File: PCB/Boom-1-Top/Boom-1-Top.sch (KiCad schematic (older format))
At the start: 983 parts, among them J1 DEBUG, J10 PIC_DEBUG, J11 PIC_DEBUG, J12 PIC_DEBUG, J13 PIC_DEBUG, J14 PIC_DEBUG, J15 USB_B_Micro, J16 SD_Card, J17 BT_DEBUG, J18 12V Supply, J19 3V3 Bypass, J2 MIDI IN, J20 5V Bypass, J21 Env +12V Supply, J22 Env -12V Supply, J23 OLEDConn, J3 MIDI OUT, J37 Osc1Conn, J38 Osc2Conn, J39 SubNoiseConn, J4 PIC_DEBUG, J40 FiltConn2, J41 EnvGenConn2, J42 EnvGenConn1, J43 FXConn1, J44 FiltConn1, J45 FXConn2, J46 EnvGenConn3, J5 PIC_DEBUG, J6 PIC_DEBUG, J7 PIC_DEBUG, J8 PIC_DEBUG, J9 PIC_DEBUG, Q1 AO3401A, Q2 AO3401A, SW1 Osc1SawEncoder, SW10 SubToOsc2FiltEncoder, SW11 Osc1ToOsc2FiltEncoder, SW12 Osc1FiltFreqEncoder, SW13 Osc2FiltFreqEncoder, SW14 SubFiltFreqEncoder, SW15 OscFiltEnvAttackEncoder, SW16 SubFiltEnvAttackEncoder, SW17 Osc1FiltResEncoder, SW18 Osc2FiltResEncoder, SW19 SubFiltResEncoder, SW2 Osc1SqrEncoder, SW20 OscFiltEnvDecayEncoder, SW21 SubFiltEnvDecayEncoder, SW22 OscFiltEnvSustainEncoder, SW23 SubFiltEnvSustainEncoder, SW24 Osc1DriveEncoder, SW25 Osc2DistortionEncoder, SW26 OscFiltEnvReleaseEncoder, SW27 SubFiltEnvReleaseEncoder, SW28 FXWetDryEncoder, SW29 SubAmpEnvAttackEncoder, SW3 Rotary_Encoder, SW30 OscAmpEnvAttackEncoder, SW31 FXControl1Encoder, SW32 SubAmpEnvDecayEncoder, SW33 OscAmpEnvDecayEncoder, SW34 FXControl2Encoder, SW35 SubAmpEnvSustainEncoder, SW36 OscAmpEnvSustainEncoder, SW37 FXControl3Encoder, SW38 FXFeedbackEncoder, SW39 SubAmpEnvReleaseEncoder, SW4 Rotary_Encoder_Switch, SW40 OscAmpEnvReleaseEncoder, SW41 Reset, SW42 SW_Push, SW43 Reset, SW44 SW_Push, SW45 SW_Push, SW46 SW_Push, SW47 SW_Push, SW48 SW_Push, SW49 SW_Push, SW5 Rotary_Encoder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

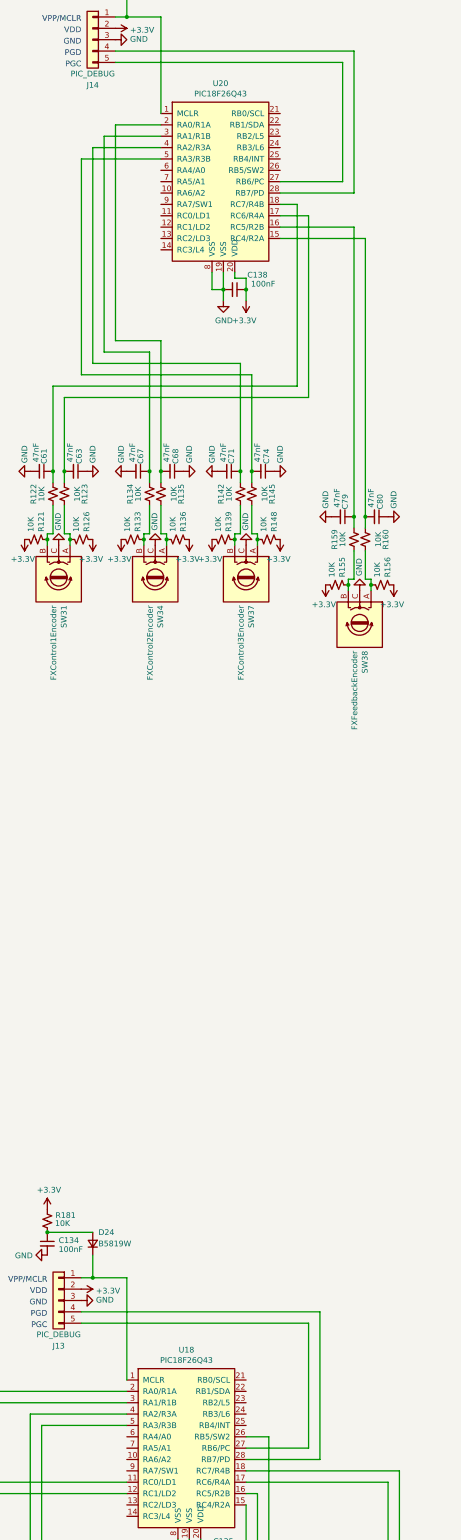
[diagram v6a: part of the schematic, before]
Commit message: U18 PIC i2c
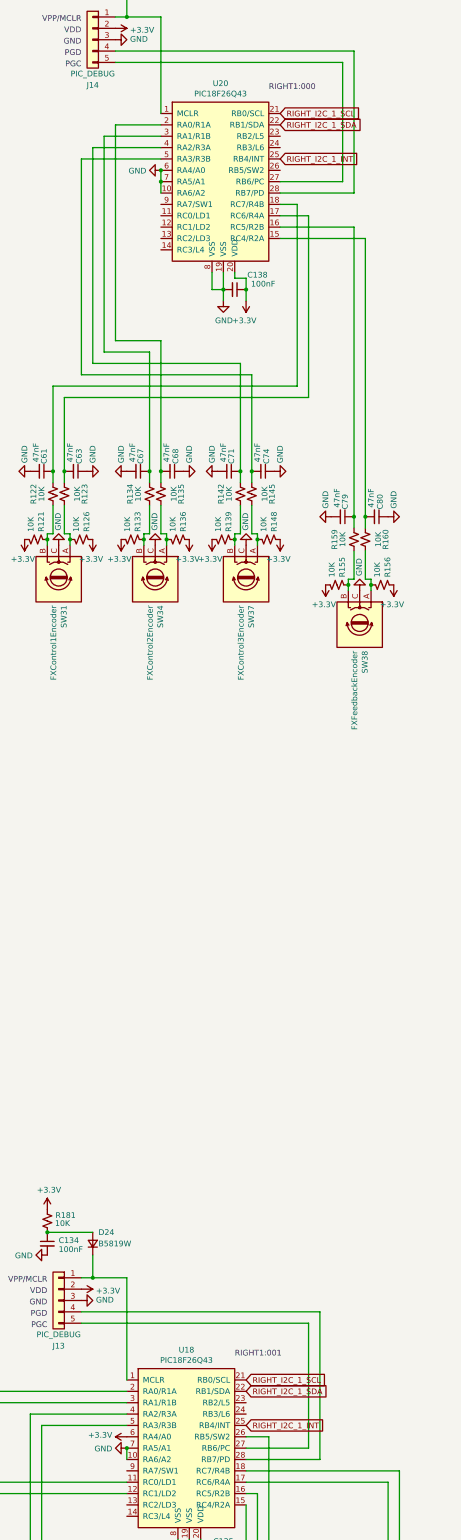
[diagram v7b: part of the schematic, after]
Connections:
- net +3V3: now also U18.6 (RA4/A0)
- net GND: now also U18.10 (RA6/A2), U18.7 (RA5/A1), U20.10 (RA6/A2), U20.6 (RA4/A0), U20.7 (RA5/A1)
- net RIGHT_I2C_1_INT: now also U18.25 (RB4/INT), U20.25 (RB4/INT)
- net RIGHT_I2C_1_SCL: now also U18.21 (RB0/SCL), U20.21 (RB0/SCL)
- net RIGHT_I2C_1_SDA: now also U18.22 (RB1/SDA), U20.22 (RB1/SDA)
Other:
- note added: "RIGHT1:000"
- note added: "RIGHT1:001"
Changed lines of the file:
@@
 LEFT_I2C_3_SCL
 $Comp
-L power:GND #PWR?
+L power:GND #PWR0909
 U 1 1 62205F51
 P 37650 14650
-F 0 "#PWR?" H 37650 14400 50  0001 C CNN
+F 0 "#PWR0909" H 37650 14400 50  0001 C CNN
 F 1 "GND" V 37655 14522 50  0000 R CNN
 F 2 "" H 37650 14650 50  0001 C CNN
@@
 RIGHT0:000
 $Comp
-L power:GND #PWR?
+L power:GND #PWR0910
 U 1 1 60DF9D17
 P 44250 3050
-F 0 "#PWR?" H 44250 2800 50  0001 C CNN
+F 0 "#PWR0910" H 44250 2800 50  0001 C CNN
 F 1 "GND" V 44255 2922 50  0000 R CNN
 F 2 "" H 44250 3050 50  0001 C CNN
@@
 Wire Wire Line
 	44250 3150 44250 3250
+Text Notes 45500 14450 0    50   ~ 0
+RIGHT1:000
+Text GLabel 45600 15050 2    50   Input ~ 0
+RIGHT_I2C_1_INT
+Text GLabel 45600 14750 2    50   Input ~ 0
+RIGHT_I2C_1_SDA
+Text GLabel 45600 14650 2    50   Input ~ 0
+RIGHT_I2C_1_SCL
+$Comp
+L power:GND #PWR0911
+U 1 1 61AEE9F7
+P 44550 15150
+F 0 "#PWR0911" H 44550 14900 50  0001 C CNN
+F 1 "GND" V 44555 15022 50  0000 R CNN
+F 2 "" H 44550 15150 50  0001 C CNN
+F 3 "" H 44550 15150 50  0001 C CNN
+	1    44550 15150
+	0    1    1    0
+$EndComp
+Wire Wire Line
+	44550 15150 44550 15250
+Connection ~ 44550 15150
+Connection ~ 44550 15250
+Wire Wire Line
+	44550 15250 44550 15350
+Text Notes 45200 25600 0    50   ~ 0
+RIGHT1:001
+Text GLabel 45300 26200 2    50   Input ~ 0
+RIGHT_I2C_1_INT
+Text GLabel 45300 25900 2    50   Input ~ 0
+RIGHT_I2C_1_SDA
+Text GLabel 45300 25800 2    50   Input ~ 0
+RIGHT_I2C_1_SCL
+$Comp
+L power:+3.3V #PWR?
+U 1 1 625EF341
+P 44250 26300
+F 0 "#PWR?" H 44250 26150 50  0001 C CNN
+F 1 "+3.3V" V 44265 26428 50  0000 L CNN
+F 2 "" H 44250 26300 50  0001 C CNN
+F 3 "" H 44250 26300 50  0001 C CNN
+	1    44250 26300
+	0    -1   -1   0
+$EndComp
+$Comp
+L power:GND #PWR?
+U 1 1 625FB100
+P 44250 26400
+F 0 "#PWR?" H 44250 26150 50  0001 C CNN
+F 1 "GND" V 44255 26272 50  0000 R CNN
+F 2 "" H 44250 26400 50  0001 C CNN
+F 3 "" H 44250 26400 50  0001 C CNN
+	1    44250 26400
+	0    1    1    0
+$EndComp
+Wire Wire Line
+	44250 26400 44250 26500
+Connection ~ 44250 26400
 $EndSCHEMATC

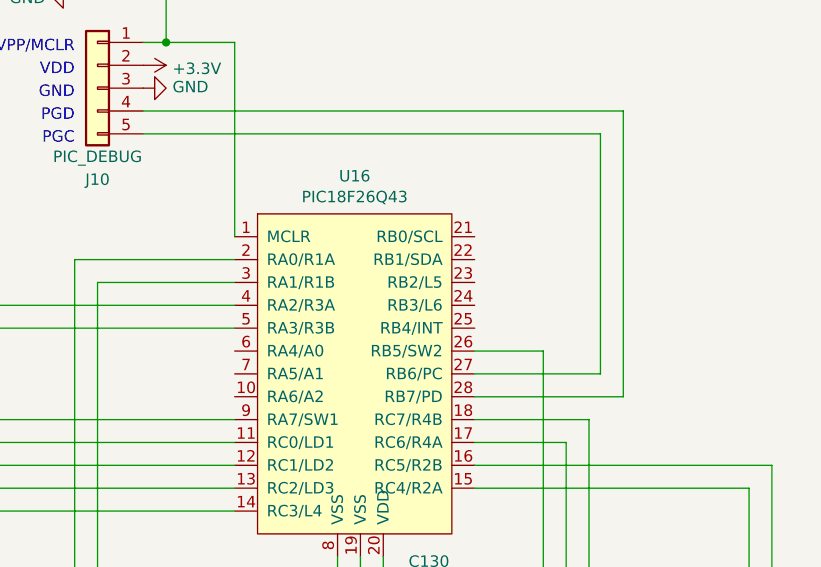
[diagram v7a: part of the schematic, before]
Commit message: U16 PIC i2c
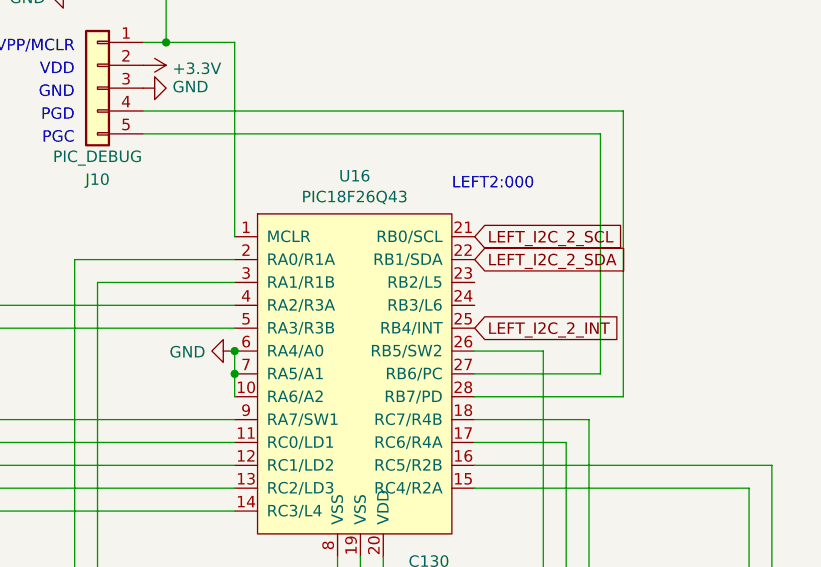
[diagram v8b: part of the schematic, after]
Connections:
- net GND: now also U16.10 (RA6/A2), U16.6 (RA4/A0), U16.7 (RA5/A1)
- net LEFT_I2C_2_INT: now also U16.25 (RB4/INT)
- net LEFT_I2C_2_SCL: now also U16.21 (RB0/SCL)
- net LEFT_I2C_2_SDA: now also U16.22 (RB1/SDA)
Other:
- note added: "LEFT2:000"
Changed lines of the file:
@@
 RIGHT_I2C_1_SCL
 $Comp
-L power:+3.3V #PWR?
+L power:+3.3V #PWR0912
 U 1 1 625EF341
 P 44250 26300
-F 0 "#PWR?" H 44250 26150 50  0001 C CNN
+F 0 "#PWR0912" H 44250 26150 50  0001 C CNN
 F 1 "+3.3V" V 44265 26428 50  0000 L CNN
 F 2 "" H 44250 26300 50  0001 C CNN
@@
 $EndComp
 $Comp
-L power:GND #PWR?
+L power:GND #PWR0913
 U 1 1 625FB100
 P 44250 26400
-F 0 "#PWR?" H 44250 26150 50  0001 C CNN
+F 0 "#PWR0913" H 44250 26150 50  0001 C CNN
 F 1 "GND" V 44255 26272 50  0000 R CNN
 F 2 "" H 44250 26400 50  0001 C CNN
@@
 	44250 26400 44250 26500
 Connection ~ 44250 26400
+Text Notes 38550 21800 0    50   ~ 0
+LEFT2:000
+Text GLabel 38650 22400 2    50   Input ~ 0
+LEFT_I2C_2_INT
+Text GLabel 38650 22100 2    50   Input ~ 0
+LEFT_I2C_2_SDA
+Text GLabel 38650 22000 2    50   Input ~ 0
+LEFT_I2C_2_SCL
+$Comp
+L power:GND #PWR?
+U 1 1 63216B9C
+P 37600 22500
+F 0 "#PWR?" H 37600 22250 50  0001 C CNN
+F 1 "GND" V 37605 22372 50  0000 R CNN
+F 2 "" H 37600 22500 50  0001 C CNN
+F 3 "" H 37600 22500 50  0001 C CNN
+	1    37600 22500
+	0    1    1    0
+$EndComp
+Wire Wire Line
+	37600 22500 37600 22600
+Connection ~ 37600 22500
+Connection ~ 37600 22600
+Wire Wire Line
+	37600 22600 37600 22700
 $EndSCHEMATC
